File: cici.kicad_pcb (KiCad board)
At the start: 2 copper layers, 88.4 x 132.8 mm, 38 parts, among them SW1 SW_PUSH, SW10 SW_PUSH, SW11 SW_PUSH, SW12 SW_PUSH, SW13 SW_PUSH, SW14 SW_PUSH, SW15 SW_PUSH, SW16 SW_PUSH, SW17 SW_PUSH, SW18 SW_PUSH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

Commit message: realizzato bottom e sistemato fori per viti
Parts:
- added Ref**: Val**, MountingHole:MountingHole_2.2mm_M2_Pad, F.Cu at (94.2, 146.0)
- added Ref**: Val**, MountingHole:MountingHole_2.2mm_M2_Pad, F.Cu at (134.2, 30.1)
- added Ref**: Val**, MountingHole:MountingHole_2.2mm_M2_Pad, F.Cu at (54.1, 30.1)
- added Ref**: Val**, MountingHole:MountingHole_2.2mm_M2_Pad, F.Cu at (120.8, 135.0)
- added Ref**: Val**, MountingHole:MountingHole_2.2mm_M2_Pad, F.Cu at (67.4, 135.0)
- added Ref**: Val**, MountingHole:MountingHole_2.2mm_M2_Pad, F.Cu at (94.1, 89.9)
- added Ref**: Val**, MountingHole:MountingHole_2.2mm_M2_Pad, F.Cu at (113.1, 70.8)
- added Ref**: Val**, MountingHole:MountingHole_2.2mm_M2_Pad, F.Cu at (75.0, 70.8)
- added SW_R1: SW_PUSH, kbd:ResetSW_1side, F.Cu at (97.2, 31.0)
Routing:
- net GND: track 48.2 -> 57.5 mm
- net reset: track 49.1 -> 39.8 mm, vias 0 -> 1
- net row2: track 82.0 -> 86.8 mm
- net Net-(D1-Pad2): track 56.7 -> 55.5 mm
- net row1: track 68.7 -> 69.8 mm
- net row4: track 67.5 -> 68.1 mm

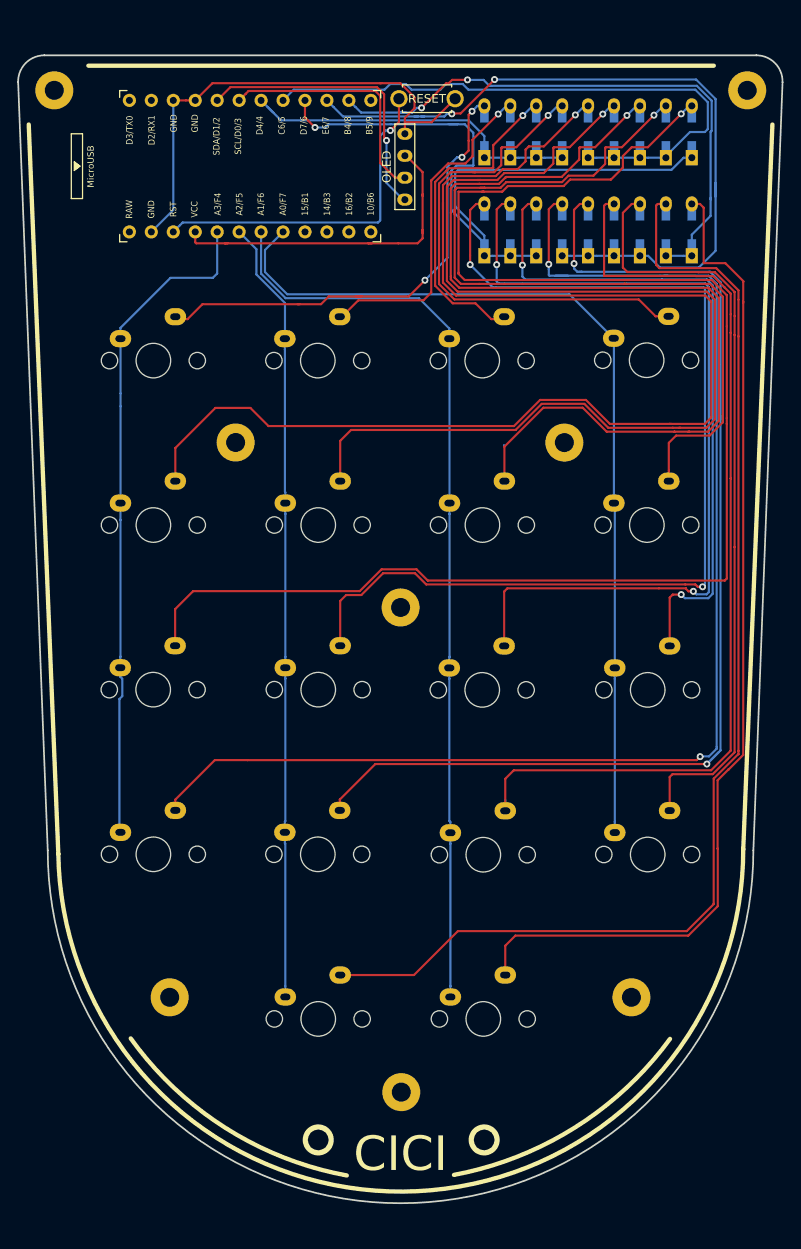
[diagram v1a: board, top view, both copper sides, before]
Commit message: creazione pezzo acrilico e sistemazione fori
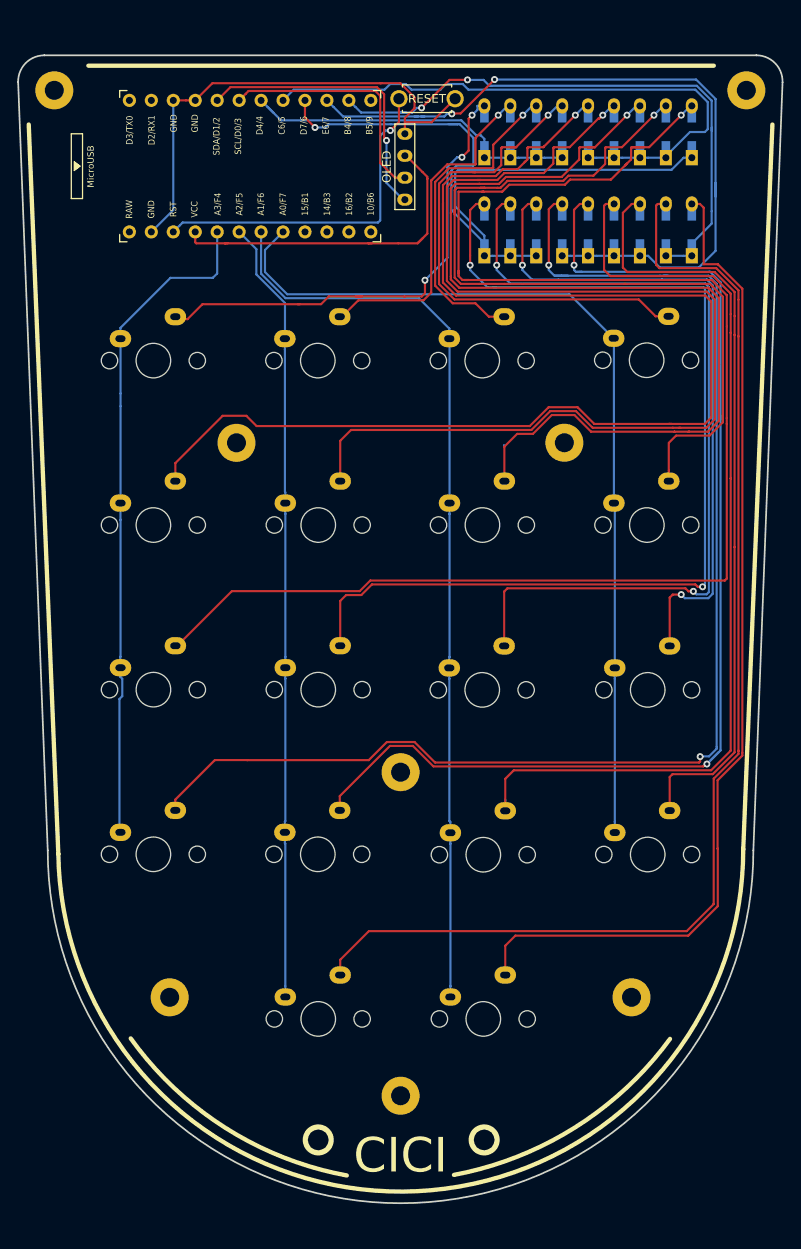
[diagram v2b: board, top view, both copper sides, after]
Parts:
- moved Ref** 19.1 mm to (94.1, 109.0)
- moved Ref** 0.43 mm to (94.1, 146.4)
- moved e 0.11 mm to (75.1, 70.8)
- moved Ref** 0.10 mm to (134.1, 30.1)
- renumbered Ref** to e
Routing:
- net row1: track 69.8 -> 74.7 mm
- net row3: track 87.4 -> 92.3 mm
- net Net-(D14-Pad2): track 130.6 -> 134.1 mm
- net row0: track 40.2 -> 43.6 mm
- net row2: track 86.8 -> 90.2 mm
- net Net-(D13-Pad2): track 152.5 -> 155.7 mm
- net Net-(D4-Pad2): track 59.2 -> 61.6 mm
- net Net-(D2-Pad2): track 38.6 -> 40.9 mm
- net Net-(D17-Pad2): track 137.7 -> 139.9 mm
- net Net-(D1-Pad2): track 55.5 -> 57.6 mm
- net Net-(D7-Pad2): track 116.1 -> 117.9 mm
- net Net-(D3-Pad2): track 38.7 -> 40.3 mm
- net row4: track 68.1 -> 69.4 mm
- net Net-(D8-Pad2): track 100.1 -> 101.3 mm
- net Net-(D16-Pad2): track 88.7 -> 89.9 mm
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
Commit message: creazione gerber e conclusione primo tentativo
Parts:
- moved SW15 0.08 mm to (103.6, 118.5)
- moved SW6 0.05 mm to (84.5, 80.4)
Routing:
- net row2: track 90.2 -> 84.7 mm
- net Net-(D1-Pad2): track 57.6 -> 58.8 mm
- net Net-(D15-Pad2): track 111.0 -> 111.9 mm
- net Net-(D16-Pad2): track 89.9 -> 89.1 mm
- net Net-(D17-Pad2): track 139.9 -> 140.6 mm
- net row1: track 74.7 -> 74.1 mm

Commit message: prima versione conclusa. inizio seconda
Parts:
- removed Ref** (x7), e: Val**, MountingHole:MountingHole_2.2mm_M2_Pad
- added REF**: MountingHole_2.2mm_M2_Pad, MountingHole:MountingHole_2.2mm_M2_Pad, F.Cu at (54.1, 25.5)
- added REF**: MountingHole_2.2mm_M2_Pad, MountingHole:MountingHole_2.2mm_M2_Pad, F.Cu at (94.1, 109.0)
- added REF**: MountingHole_2.2mm_M2_Pad, MountingHole:MountingHole_2.2mm_M2_Pad, F.Cu at (75.1, 70.8)
- added REF**: MountingHole_2.2mm_M2_Pad, MountingHole:MountingHole_2.2mm_M2_Pad, F.Cu at (113.1, 70.8)
- added REF**: MountingHole_2.2mm_M2_Pad, MountingHole:MountingHole_2.2mm_M2_Pad, F.Cu at (94.1, 146.4)
- added REF**: MountingHole_2.2mm_M2_Pad, MountingHole:MountingHole_2.2mm_M2_Pad, F.Cu at (67.4, 135.0)
- added REF**: MountingHole_2.2mm_M2_Pad, MountingHole:MountingHole_2.2mm_M2_Pad, F.Cu at (134.1, 25.5)
- added REF**: MountingHole_2.2mm_M2_Pad, MountingHole:MountingHole_2.2mm_M2_Pad, F.Cu at (120.8, 135.0)
- D1, D10, D11, D12, D13, D14, D15, D16, D17, D18, D2, D3, D4, D5, D6, D7, D8, D9: moved to F.Cu
- moved U1 7.59 mm to (69.7, 39.4)
- moved OLED1 7.17 mm to (87.5, 43.2)
- moved D1 4.98 mm to (101.7, 30.3)
- moved D10 4.98 mm to (101.7, 41.7)
- moved D11 4.98 mm to (104.7, 41.7)
- moved D12 4.98 mm to (107.7, 41.7)
- moved D13 4.98 mm to (110.7, 41.7)
- moved D14 4.98 mm to (113.7, 41.7)
- moved D15 4.98 mm to (116.7, 41.7)
- moved D16 4.98 mm to (119.7, 41.7)
- moved D17 4.98 mm to (122.7, 41.7)
- moved D18 4.98 mm to (125.7, 41.7)
- moved D2 4.98 mm to (104.7, 30.3)
- moved D3 4.98 mm to (107.7, 30.3)
- moved D4 4.98 mm to (110.7, 30.3)
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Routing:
- net row2: track 84.7 -> 112.8 mm
- net Net-(D9-Pad2): track 177.5 -> 153.2 mm, vias 1 -> 2
- net row3: track 92.3 -> 75.5 mm, vias 2 -> 1
- net Net-(D1-Pad2): track 58.8 -> 75.4 mm, vias 3 -> 2
- net row0: track 43.6 -> 60.2 mm, vias 0 -> 1
- net VCC: track 40.1 -> 28.4 mm
- net row4: track 69.1 -> 78.5 mm, vias 2 -> 3
- net Net-(D4-Pad2): track 61.6 -> 70.9 mm, vias 1 -> 2
- net Net-(D3-Pad2): track 40.3 -> 49.3 mm, vias 1 -> 2
- net Net-(D5-Pad2): track 150.4 -> 159.2 mm, vias 1 -> 2
- net Net-(D7-Pad2): track 117.9 -> 126.4 mm, vias 1 -> 2
- net Net-(D6-Pad2): track 133.7 -> 141.4 mm, vias 1 -> 2
- net Net-(D14-Pad2): track 134.1 -> 141.3 mm
- net Net-(D8-Pad2): track 101.3 -> 108.5 mm, vias 1 -> 2
- net Net-(D12-Pad2): track 79.9 -> 86.9 mm
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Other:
- board size 88.4 x 132.8 mm -> 88.4 x 140.3 mm
